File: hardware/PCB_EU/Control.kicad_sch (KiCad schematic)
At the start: 27 parts, among them U801 TC4427AEPA, U802 LM2903D-ST

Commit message: hardware: apply PCB_EU review fixes
- R702 100k -> 4k7: ESP32 internal pull-up on GPIO32 (old firmware
  INPUT_PULLUP) could switch the 100 W PTC on.
- C208 100n -> 1u for the Espressif EN delay.
- Remove TC4427A driver and its parts; each LM3429 GATE drives its own
  IRF540Z through 4R7 (driver was 20-25 mm from both MOSFETs).
- Add reverse-polarity protection: Q102 IRF1010ES in the input return
  with a 5k6+5k6 / 10k gate divider.
- F103 label: UST 1206 is time-lag.
- Rebuild PCB via build_board.py + route_power.py, rerun all checks on
  KiCad 10.0.7: ERC 0, DRC 0 / parity 0, 355 unrouted, 51 checks.
- Parts estimate 80.00 -> 78.59 EUR; check ceiling raised to 100 EUR.

Co-Authored-By: Claude Opus 5.5 (1M context) <noreply@anthropic.com>
Claude-Session: https://claude.ai/code/session_01AxccZX6Cb4FnRKJMrFYMSX
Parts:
- removed C801: 10u 25V, Capacitor_SMD:C_1206_3216Metric, symbol EU:C
- removed C802: 100n, Capacitor_SMD:C_0805_2012Metric, symbol EU:C
- removed R801, R805: 1k, Resistor_SMD:R_0603_1608Metric, symbol EU:R
- removed R802, R806: 100k, Resistor_SMD:R_0603_1608Metric, symbol EU:R
- removed U801: TC4427AEPA, Package_DIP:DIP-8_W7.62mm, symbol EU:TC4427A
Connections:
- net LED1_TC_OUT is gone; now on net LED1_GATE_RAW: R803.1
- net LED2_TC_OUT is gone; now on net LED2_GATE_RAW: R807.1
- no-connect marks 4 -> 2
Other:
- moved on the sheet: C803, D801, R803, R804, R807, R808, R809, R810, R811, R812, R813, R814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

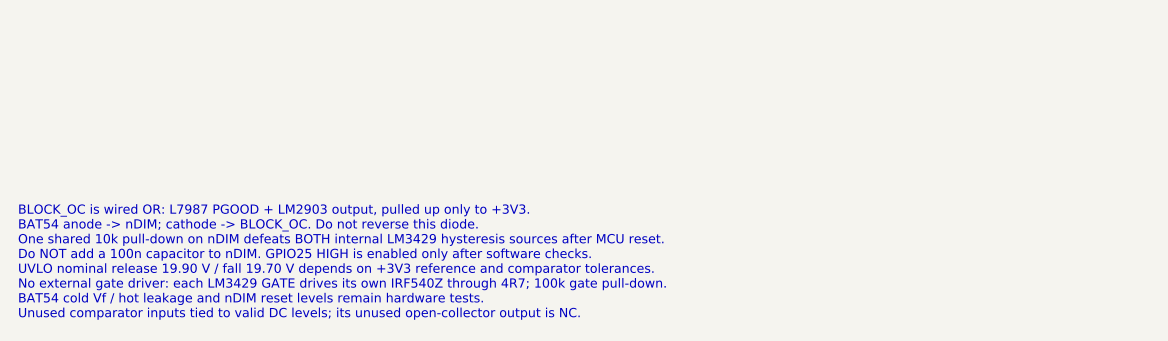
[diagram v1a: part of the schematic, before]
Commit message: PCB_EU: hand-route LED2 power loop, 5 mm cap footprint, TK22E10N1 switches
- C508-C510, C608, C609 (EEUFR1J101LB) use CP_Radial_D8.0mm_P5.00mm, the
  real 5 mm lead pitch; the 3.5 mm footprint is removed and the 3D fit check
  has no known issues left.
- LED2 is placed and routed like LED1: R601 under Q601, D601 anodes toward
  the switch, C611 between C609 leads, wide SW/IS/OUT/GND copper, LED+ and
  the gate on In2. Eight new connected groups are checked.
- route_board.py drops session copper of nets the plan now routes
  (replace_session_nets) and session vias that break hole spacing, and no
  longer prunes GND stitching vias before the pours exist.
- Q501/Q601: IRF540Z -> Toshiba TK22E10N1 (28 nC instead of 42 nC gate
  charge for the 7 V LM3429 driver); BOM 78.59 -> 77.95 EUR.

0 unrouted, DRC 0, schematic parity 0; rebuild is byte-identical.

Co-Authored-By: Claude Opus 5.5 (1M context) <noreply@anthropic.com>
Claude-Session: https://claude.ai/code/session_01AxccZX6Cb4FnRKJMrFYMSX
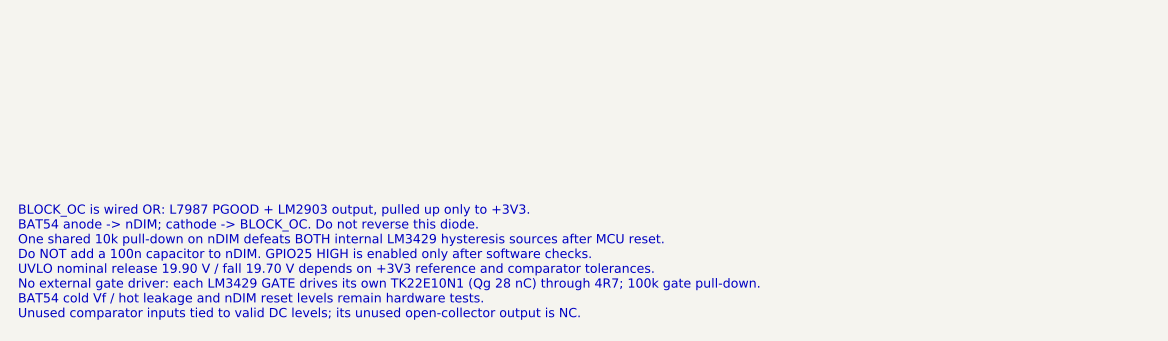
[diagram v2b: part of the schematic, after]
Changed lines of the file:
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@@
 (kicad_sch (version 20260306) (generator "eeschema") (generator_version "10.0") (paper "A3") (title_block (title "08 | LED gate drive and hardware inhibit") (date "2026-10-20") (rev "EU-0.1") (company "GrowBox | EU prototype") (comment 1 "SCHEMATIC DRAFT | PARTIAL LED1 PCB ROUTING | no manufacturing release"))
 (text "08 | LED gate drive and hardware inhibit" (at 12.7 12.7 0) (effects (font (size 2 2)) (justify left top)))
-(text "BLOCK_OC is wired OR: L7987 PGOOD + LM2903 output, pulled up only to +3V3.\nBAT54 anode -> nDIM; cathode -> BLOCK_OC. Do not reverse this diode.\nOne shared 10k pull-down on nDIM defeats BOTH internal LM3429 hysteresis sources after MCU reset.\nDo NOT add a 100n capacitor to nDIM. GPIO25 HIGH is enabled only after software checks.\nUVLO nominal release 19.90 V / fall 19.70 V depends on +3V3 reference and comparator tolerances.\nNo external gate driver: each LM3429 GATE drives its own IRF540Z through 4R7; 100k gate pull-down.\nBAT54 cold Vf / hot leakage and nDIM reset levels remain hardware tests.\nUnused comparator inputs tied to valid DC levels; its unused open-collector output is NC." (at 12.7 251 0) (effects (font (size 1.02 1.02)) (justify left top)))
+(text "BLOCK_OC is wired OR: L7987 PGOOD + LM2903 output, pulled up only to +3V3.\nBAT54 anode -> nDIM; cathode -> BLOCK_OC. Do not reverse this diode.\nOne shared 10k pull-down on nDIM defeats BOTH internal LM3429 hysteresis sources after MCU reset.\nDo NOT add a 100n capacitor to nDIM. GPIO25 HIGH is enabled only after software checks.\nUVLO nominal release 19.90 V / fall 19.70 V depends on +3V3 reference and comparator tolerances.\nNo external gate driver: each LM3429 GATE drives its own TK22E10N1 (Qg 28 nC) through 4R7; 100k gate pull-down.\nBAT54 cold Vf / hot leakage and nDIM reset levels remain hardware tests.\nUnused comparator inputs tied to valid DC levels; its unused open-collector output is NC." (at 12.7 251 0) (effects (font (size 1.02 1.02)) (justify left top)))
 (symbol (lib_id "EU:R") (at 45.72 119.38 0) (unit 1) (in_bom yes) (on_board yes) (dnp no)
 (property "Reference" "R803" (at 45.72 113.74 0) (effects (font (size 1.15 1.15)) ))

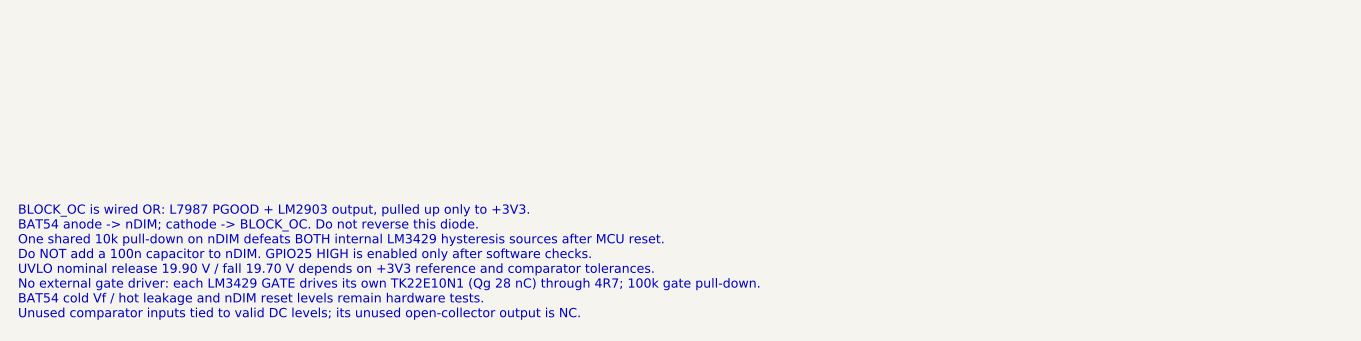
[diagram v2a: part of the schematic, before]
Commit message: PCB_EU: Q601 CSD19534KCS, Q102/Q703 FDB5800, BOM updated
Q601 (LED2 boost switch, no heatsink): TK22E10N1 -> TI CSD19534KCS on the
same TO-220 land. Q102 (reverse polarity) and Q703 (PTC switch):
IRF1010ESPBF -> onsemi FDB5800 on the same TO-263-2 land. Q501 stays
TK22E10N1.

BOM 82.50 -> 85.75 EUR: FDB5800 x2 Salvats 3.96 (was IRF 2.42),
TK22E10N1 x1 instead of x2 (-1.38), CSD19534KCS x1 Electrobase 3.09.
Shipping 5.87 and the two parcels are unchanged.

tools/generate.py rebuilds schematics, design.json and the BOM (the
generator is idempotent). Value/Datasheet/MPN/Design_note of the three
parts are text-patched in PCB_EU.kicad_pcb and review/netlist.xml the way
a KiCad export and build_board.py would write them; review/connectivity.txt
comes from tools/verify.py (56 checks pass). DESIGN.md and README.md are
updated.

KiCad was not run: ERC, DRC, schematic parity and the other KiCad-based
checks of run_checks.py have NOT been run for this commit.

Co-Authored-By: Claude Sonnet 5.5 <noreply@anthropic.com>
Claude-Session: https://claude.ai/code/session_011GxPyRnAFpBjFQ5VURqV5H
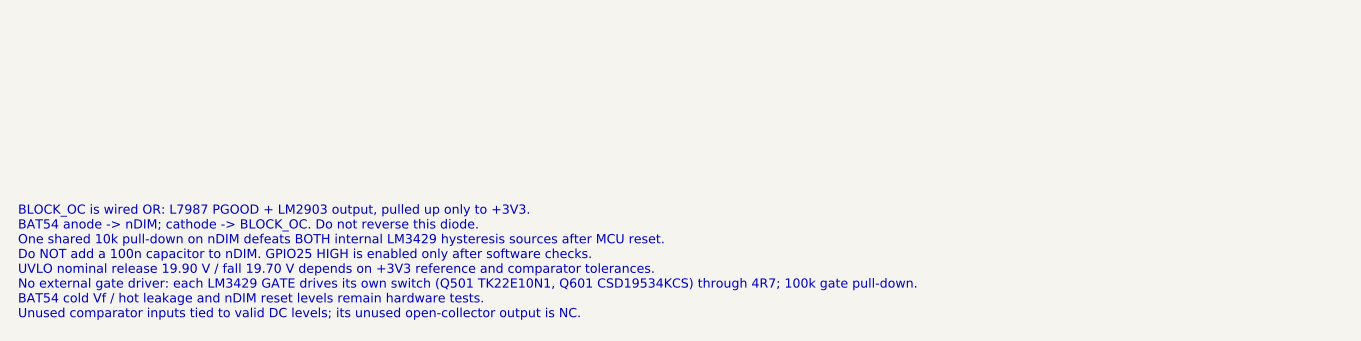
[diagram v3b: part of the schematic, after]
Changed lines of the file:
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@@
 (kicad_sch (version 20260306) (generator "eeschema") (generator_version "10.0") (paper "A3") (title_block (title "08 | LED gate drive and hardware inhibit") (date "2026-10-20") (rev "EU-0.1") (company "GrowBox | EU prototype") (comment 1 "SCHEMATIC DRAFT | PARTIAL LED1 PCB ROUTING | no manufacturing release"))
 (text "08 | LED gate drive and hardware inhibit" (at 12.7 12.7 0) (effects (font (size 2 2)) (justify left top)))
-(text "BLOCK_OC is wired OR: L7987 PGOOD + LM2903 output, pulled up only to +3V3.\nBAT54 anode -> nDIM; cathode -> BLOCK_OC. Do not reverse this diode.\nOne shared 10k pull-down on nDIM defeats BOTH internal LM3429 hysteresis sources after MCU reset.\nDo NOT add a 100n capacitor to nDIM. GPIO25 HIGH is enabled only after software checks.\nUVLO nominal release 19.90 V / fall 19.70 V depends on +3V3 reference and comparator tolerances.\nNo external gate driver: each LM3429 GATE drives its own TK22E10N1 (Qg 28 nC) through 4R7; 100k gate pull-down.\nBAT54 cold Vf / hot leakage and nDIM reset levels remain hardware tests.\nUnused comparator inputs tied to valid DC levels; its unused open-collector output is NC." (at 12.7 251 0) (effects (font (size 1.02 1.02)) (justify left top)))
+(text "BLOCK_OC is wired OR: L7987 PGOOD + LM2903 output, pulled up only to +3V3.\nBAT54 anode -> nDIM; cathode -> BLOCK_OC. Do not reverse this diode.\nOne shared 10k pull-down on nDIM defeats BOTH internal LM3429 hysteresis sources after MCU reset.\nDo NOT add a 100n capacitor to nDIM. GPIO25 HIGH is enabled only after software checks.\nUVLO nominal release 19.90 V / fall 19.70 V depends on +3V3 reference and comparator tolerances.\nNo external gate driver: each LM3429 GATE drives its own switch (Q501 TK22E10N1, Q601 CSD19534KCS) through 4R7; 100k gate pull-down.\nBAT54 cold Vf / hot leakage and nDIM reset levels remain hardware tests.\nUnused comparator inputs tied to valid DC levels; its unused open-collector output is NC." (at 12.7 251 0) (effects (font (size 1.02 1.02)) (justify left top)))
 (symbol (lib_id "EU:R") (at 45.72 119.38 0) (unit 1) (in_bom yes) (on_board yes) (dnp no)
 (property "Reference" "R803" (at 45.72 113.74 0) (effects (font (size 1.15 1.15)) ))
